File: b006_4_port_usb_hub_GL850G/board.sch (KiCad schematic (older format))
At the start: 37 parts, among them J1 008_USB_2x2, J2 GL850G, J3 008_USB_2x2, J4 008_USB_2x2, J5 008_USB_2x2, J6 008_USB_2x2, Y1 12MhZ

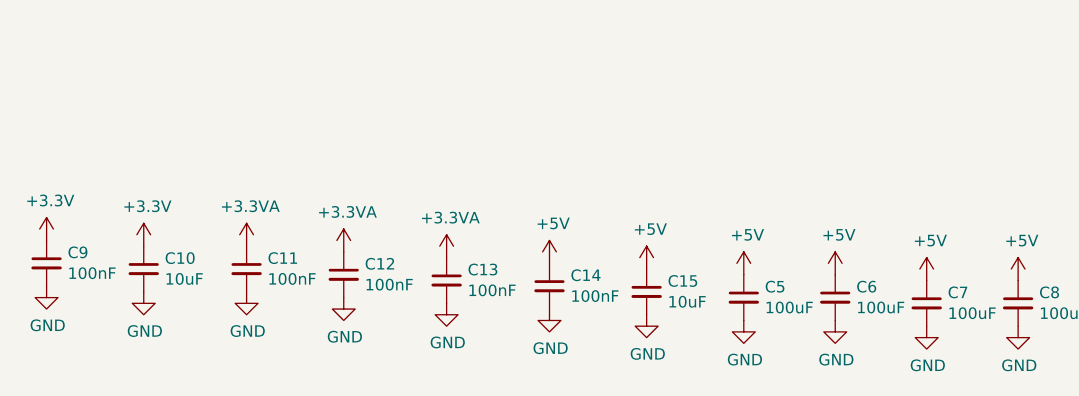
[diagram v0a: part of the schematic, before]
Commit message: added part info for silicon parts
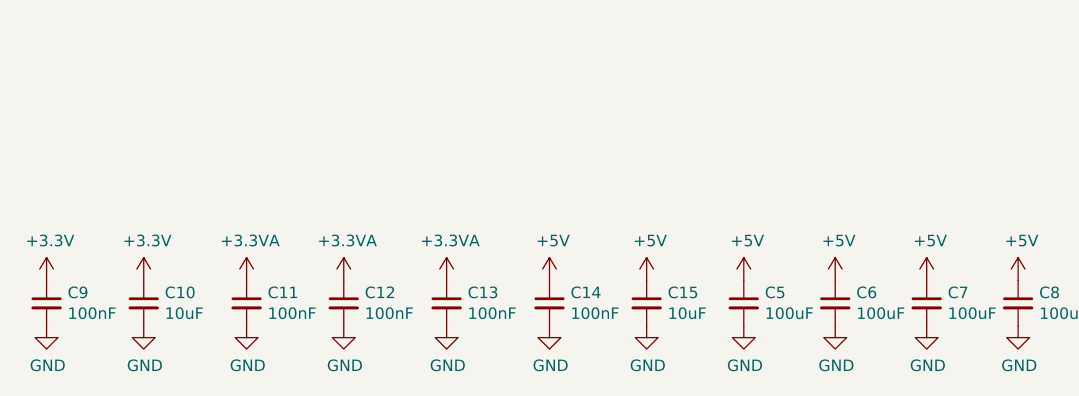
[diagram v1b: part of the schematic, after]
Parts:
- J2: MPN (none) -> GL850G
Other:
- moved on the sheet: C10, C11, C12, C13, C14, C15, C5, C6, C9

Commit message: updated usb plugs
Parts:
- J1: footprint on_edge:on_edge_2x02_device -> on_edge:on_edge_2x05_device
- J3, J4, J5, J6: footprint on_edge:on_edge_2x02_host -> on_edge:on_edge_2x05_host
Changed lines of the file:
@@
 F 0 "J1" H 3378 3088 50  0000 L CNN
 F 1 "008_USB_2x2" H 3378 2997 50  0000 L CNN
-F 2 "on_edge:on_edge_2x02_device" H 3350 3725 50  0001 C CNN
+F 2 "on_edge:on_edge_2x05_device" H 3350 3725 50  0001 C CNN
 F 3 "" H 3350 3725 50  0001 C CNN
 	1    3050 3075
@@
 F 0 "J5" H 10228 1188 50  0000 L CNN
 F 1 "008_USB_2x2" H 10228 1097 50  0000 L CNN
-F 2 "on_edge:on_edge_2x02_host" H 10200 1825 50  0001 C CNN
+F 2 "on_edge:on_edge_2x05_host" H 10200 1825 50  0001 C CNN
 F 3 "" H 10200 1825 50  0001 C CNN
 	1    9900 1175
@@
 F 0 "J6" H 10253 2663 50  0000 L CNN
 F 1 "008_USB_2x2" H 10253 2572 50  0000 L CNN
-F 2 "on_edge:on_edge_2x02_host" H 10225 3300 50  0001 C CNN
+F 2 "on_edge:on_edge_2x05_host" H 10225 3300 50  0001 C CNN
 F 3 "" H 10225 3300 50  0001 C CNN
 	1    9925 2650
@@
 F 0 "J4" H 10203 4138 50  0000 L CNN
 F 1 "008_USB_2x2" H 10203 4047 50  0000 L CNN
-F 2 "on_edge:on_edge_2x02_host" H 10175 4775 50  0001 C CNN
+F 2 "on_edge:on_edge_2x05_host" H 10175 4775 50  0001 C CNN
 F 3 "" H 10175 4775 50  0001 C CNN
 	1    9875 4125
@@
 F 0 "J3" H 10178 5638 50  0000 L CNN
 F 1 "008_USB_2x2" H 10178 5547 50  0000 L CNN
-F 2 "on_edge:on_edge_2x02_host" H 10150 6275 50  0001 C CNN
+F 2 "on_edge:on_edge_2x05_host" H 10150 6275 50  0001 C CNN
 F 3 "" H 10150 6275 50  0001 C CNN
 	1    9850 5625

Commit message: added OSHW logo and updated usb connector version in schemetic
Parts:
- added l1: Logo_Open_Hardware_Large, Symbol:OSHW-Logo2_7.3x6mm_SilkScreen, symbol Graphic:Logo_Open_Hardware_Large
- J1, J3, J4, J5, J6: symbol put_on_edge:008_USB_2x2 -> put_on_edge:008_USB
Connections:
- no-connect marks 3 -> 23
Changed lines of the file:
@@
 $EndDescr
 $Comp
-L put_on_edge:008_USB_2x2 J1
+L put_on_edge:008_USB J1
 U 1 1 602ADECE
-P 3050 3075
-F 0 "J1" H 3378 3088 50  0000 L CNN
-F 1 "008_USB_2x2" H 3378 2997 50  0000 L CNN
-F 2 "on_edge:on_edge_2x05_device" H 3350 3725 50  0001 C CNN
-F 3 "" H 3350 3725 50  0001 C CNN
-	1    3050 3075
+P 3050 3275
+F 0 "J1" H 3378 3288 50  0000 L CNN
+F 1 "008_USB_2x2" H 3378 3197 50  0000 L CNN
+F 2 "on_edge:on_edge_2x05_device" H 3350 3925 50  0001 C CNN
+F 3 "" H 3350 3925 50  0001 C CNN
+	1    3050 3275
 	-1   0    0    -1
 $EndComp
 $Comp
-L put_on_edge:008_USB_2x2 J5
+L put_on_edge:008_USB J5
 U 1 1 602AEA37
-P 9900 1175
-F 0 "J5" H 10228 1188 50  0000 L CNN
-F 1 "008_USB_2x2" H 10228 1097 50  0000 L CNN
-F 2 "on_edge:on_edge_2x05_host" H 10200 1825 50  0001 C CNN
-F 3 "" H 10200 1825 50  0001 C CNN
-	1    9900 1175
-	1    0    0    -1
-$EndComp
-$Comp
-L put_on_edge:008_USB_2x2 J6
+P 10150 1375
+F 0 "J5" H 10478 1388 50  0000 L CNN
+F 1 "008_USB_2x2" H 10478 1297 50  0000 L CNN
+F 2 "on_edge:on_edge_2x05_host" H 10450 2025 50  0001 C CNN
+F 3 "" H 10450 2025 50  0001 C CNN
+	1    10150 1375
+	1    0    0    -1
+$EndComp
+$Comp
+L put_on_edge:008_USB J6
 U 1 1 602AF05A
-P 9925 2650
-F 0 "J6" H 10253 2663 50  0000 L CNN
-F 1 "008_USB_2x2" H 10253 2572 50  0000 L CNN
-F 2 "on_edge:on_edge_2x05_host" H 10225 3300 50  0001 C CNN
-F 3 "" H 10225 3300 50  0001 C CNN
-	1    9925 2650
-	1    0    0    -1
-$EndComp
-$Comp
-L put_on_edge:008_USB_2x2 J4
+P 10175 2850
+F 0 "J6" H 10503 2863 50  0000 L CNN
+F 1 "008_USB_2x2" H 10503 2772 50  0000 L CNN
+F 2 "on_edge:on_edge_2x05_host" H 10475 3500 50  0001 C CNN
+F 3 "" H 10475 3500 50  0001 C CNN
+	1    10175 2850
+	1    0    0    -1
+$EndComp
+$Comp
+L put_on_edge:008_USB J4
 U 1 1 602AF2BD
-P 9875 4125
-F 0 "J4" H 10203 4138 50  0000 L CNN
-F 1 "008_USB_2x2" H 10203 4047 50  0000 L CNN
-F 2 "on_edge:on_edge_2x05_host" H 10175 4775 50  0001 C CNN
-F 3 "" H 10175 4775 50  0001 C CNN
-	1    9875 4125
-	1    0    0    -1
-$EndComp
-$Comp
-L put_on_edge:008_USB_2x2 J3
+P 10125 4325
+F 0 "J4" H 10453 4338 50  0000 L CNN
+F 1 "008_USB_2x2" H 10453 4247 50  0000 L CNN
+F 2 "on_edge:on_edge_2x05_host" H 10425 4975 50  0001 C CNN
+F 3 "" H 10425 4975 50  0001 C CNN
+	1    10125 4325
+	1    0    0    -1
+$EndComp
+$Comp
+L put_on_edge:008_USB J3
 U 1 1 602AF525
-P 9850 5625
-F 0 "J3" H 10178 5638 50  0000 L CNN
-F 1 "008_USB_2x2" H 10178 5547 50  0000 L CNN
-F 2 "on_edge:on_edge_2x05_host" H 10150 6275 50  0001 C CNN
-F 3 "" H 10150 6275 50  0001 C CNN
-	1    9850 5625
+P 10100 5825
+F 0 "J3" H 10428 5838 50  0000 L CNN
+F 1 "008_USB_2x2" H 10428 5747 50  0000 L CNN
+F 2 "on_edge:on_edge_2x05_host" H 10400 6475 50  0001 C CNN
+F 3 "" H 10400 6475 50  0001 C CNN
+	1    10100 5825
 	1    0    0    -1
 $EndComp
@@
 L power:GND #PWR0101
 U 1 1 602B5A8D
-P 3100 3625
-F 0 "#PWR0101" H 3100 3375 50  0001 C CNN
-F 1 "GND" H 3105 3452 50  0000 C CNN
-F 2 "" H 3100 3625 50  0001 C CNN
-F 3 "" H 3100 3625 50  0001 C CNN
-	1    3100 3625
+P 2900 3825
+F 0 "#PWR0101" H 2900 3575 50  0001 C CNN
+F 1 "GND" H 2905 3652 50  0000 C CNN
+F 2 "" H 2900 3825 50  0001 C CNN
+F 3 "" H 2900 3825 50  0001 C CNN
+	1    2900 3825
 	1    0    0    -1
 $EndComp
@@
 	6000 2875 6000 1175
 Wire Wire Line
-	6000 1175 9450 1175
-Wire Wire Line
 	5900 1275 5900 2975
 Wire Wire Line
 	5900 2975 6075 2975
 Wire Wire Line
-	5900 1275 9450 1275
-Wire Wire Line
 	6975 2975 8900 2975
 Wire Wire Line
 	8900 2975 8900 2750
 Wire Wire Line
-	8900 2750 9475 2750
-Wire Wire Line
 	6975 3075 8975 3075
 Wire Wire Line
 	8975 3075 8975 2650
 Wire Wire Line
-	8975 2650 9475 2650
-Wire Wire Line
 	6975 3575 9050 3575
 Wire Wire Line
 	9050 3575 9050 4225
 Wire Wire Line
-	9050 4225 9425 4225
-Wire Wire Line
-	9425 4125 9125 4125
-Wire Wire Line
 	9125 4125 9125 3675
 Wire Wire Line
@@
 	7150 3875 7150 5725
 Wire Wire Line
-	7150 5725 9400 5725
-Wire Wire Line
 	7250 5625 7250 3975
 Wire Wire Line
 	7250 3975 6975 3975
-Wire Wire Line
-	7250 5625 9400 5625
 $Comp
 L power:GND #PWR0104
 U 1 1 602B2604
-P 9800 6175
-F 0 "#PWR0104" H 9800 5925 50  0001 C CNN
-F 1 "GND" H 9805 6002 50  0000 C CNN
-F 2 "" H 9800 6175 50  0001 C CNN
-F 3 "" H 9800 6175 50  0001 C CNN
-	1    9800 6175
+P 10250 6375
+F 0 "#PWR0104" H 10250 6125 50  0001 C CNN
+F 1 "GND" H 10255 6202 50  0000 C CNN
+F 2 "" H 10250 6375 50  0001 C CNN
+F 3 "" H 10250 6375 50  0001 C CNN
+	1    10250 6375
 	1    0    0    -1
 $EndComp
@@
 L power:GND #PWR0105
 U 1 1 602B2D61
-P 9825 4675
-F 0 "#PWR0105" H 9825 4425 50  0001 C CNN
-F 1 "GND" H 9830 4502 50  0000 C CNN
-F 2 "" H 9825 4675 50  0001 C CNN
-F 3 "" H 9825 4675 50  0001 C CNN
-	1    9825 4675
+P 10275 4875
+F 0 "#PWR0105" H 10275 4625 50  0001 C CNN
+F 1 "GND" H 10280 4702 50  0000 C CNN
+F 2 "" H 10275 4875 50  0001 C CNN
+F 3 "" H 10275 4875 50  0001 C CNN
+	1    10275 4875
 	1    0    0    -1
 $EndComp
@@
 L power:GND #PWR0106
 U 1 1 602B34AD
-P 9875 3200
-F 0 "#PWR0106" H 9875 2950 50  0001 C CNN
-F 1 "GND" H 9880 3027 50  0000 C CNN
-F 2 "" H 9875 3200 50  0001 C CNN
-F 3 "" H 9875 3200 50  0001 C CNN
-	1    9875 3200
+P 10325 3400
+F 0 "#PWR0106" H 10325 3150 50  0001 C CNN
+F 1 "GND" H 10330 3227 50  0000 C CNN
+F 2 "" H 10325 3400 50  0001 C CNN
+F 3 "" H 10325 3400 50  0001 C CNN
+	1    10325 3400
 	1    0    0    -1
 $EndComp
@@
 L power:GND #PWR0107
 U 1 1 602B3C1C
-P 9850 1725
-F 0 "#PWR0107" H 9850 1475 50  0001 C CNN
-F 1 "GND" H 9855 1552 50  0000 C CNN
-F 2 "" H 9850 1725 50  0001 C CNN
-F 3 "" H 9850 1725 50  0001 C CNN
-	1    9850 1725
+P 10300 1925
+F 0 "#PWR0107" H 10300 1675 50  0001 C CNN
+F 1 "GND" H 10305 1752 50  0000 C CNN
+F 2 "" H 10300 1925 50  0001 C CNN
+F 3 "" H 10300 1925 50  0001 C CNN
+	1    10300 1925
 	1    0    0    -1
 $EndComp
@@
 Wire Wire Line
 	9125 1400 9125 1075
-Wire Wire Line
-	9125 1075 9450 1075
 $Comp
 L power:GND #PWR0108
@@
 Wire Wire Line
 	9150 2875 9150 2550
-Wire Wire Line
-	9150 2550 9475 2550
 $Comp
 L Device:C_Small C4
@@
 Wire Wire Line
 	9225 4300 9225 4025
-Wire Wire Line
-	9225 4025 9425 4025
 $Comp
 L Device:C_Small C3
@@
 Wire Wire Line
 	9175 5825 9175 5525
-Wire Wire Line
-	9175 5525 9400 5525
 $Comp
 L Device:C_Small C8
@@
 Wire Wire Line
 	8100 4125 8100 3925
+NoConn ~ 3500 3275
+NoConn ~ 3500 3375
+NoConn ~ 3500 3475
+NoConn ~ 3500 3575
+NoConn ~ 9700 1375
+NoConn ~ 9700 1475
+NoConn ~ 9700 1575
+NoConn ~ 9700 1675
+NoConn ~ 9725 2850
+NoConn ~ 9725 2950
+NoConn ~ 9725 3050
+NoConn ~ 9725 3150
+NoConn ~ 9675 4325
+NoConn ~ 9675 4425
+NoConn ~ 9675 4525
+NoConn ~ 9675 4625
+NoConn ~ 9650 5825
+NoConn ~ 9650 5925
+NoConn ~ 9650 6025
+NoConn ~ 9650 6125
+Wire Wire Line
+	9125 1075 9700 1075
+Wire Wire Line
+	6000 1175 9700 1175
+Wire Wire Line
+	5900 1275 9700 1275
+Wire Wire Line
+	9150 2550 9725 2550
+Wire Wire Line
+	8975 2650 9725 2650
+Wire Wire Line
+	8900 2750 9725 2750
+Wire Wire Line
+	9225 4025 9675 4025
+Wire Wire Line
+	9125 4125 9675 4125
+Wire Wire Line
+	9050 4225 9675 4225
+Wire Wire Line
+	9175 5525 9650 5525
+Wire Wire Line
+	7250 5625 9650 5625
+Wire Wire Line
+	7150 5725 9650 5725
+$Comp
+L Graphic:Logo_Open_Hardware_Large l1
+U 1 1 6110E3EF
+P 6350 6950
+F 0 "l1" H 6350 7450 50  0001 C CNN
+F 1 "Logo_Open_Hardware_Large" H 6350 6550 50  0001 C CNN
+F 2 "Symbol:OSHW-Logo2_7.3x6mm_SilkScreen" H 6350 6950 50  0001 C CNN
+F 3 "~" H 6350 6950 50  0001 C CNN
+	1    6350 6950
+	1    0    0    -1
+$EndComp
 $EndSCHEMATC
